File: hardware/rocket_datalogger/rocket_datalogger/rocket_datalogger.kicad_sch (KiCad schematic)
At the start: 8 parts, among them J4 USB_C_Receptacle_USB2.0_14P

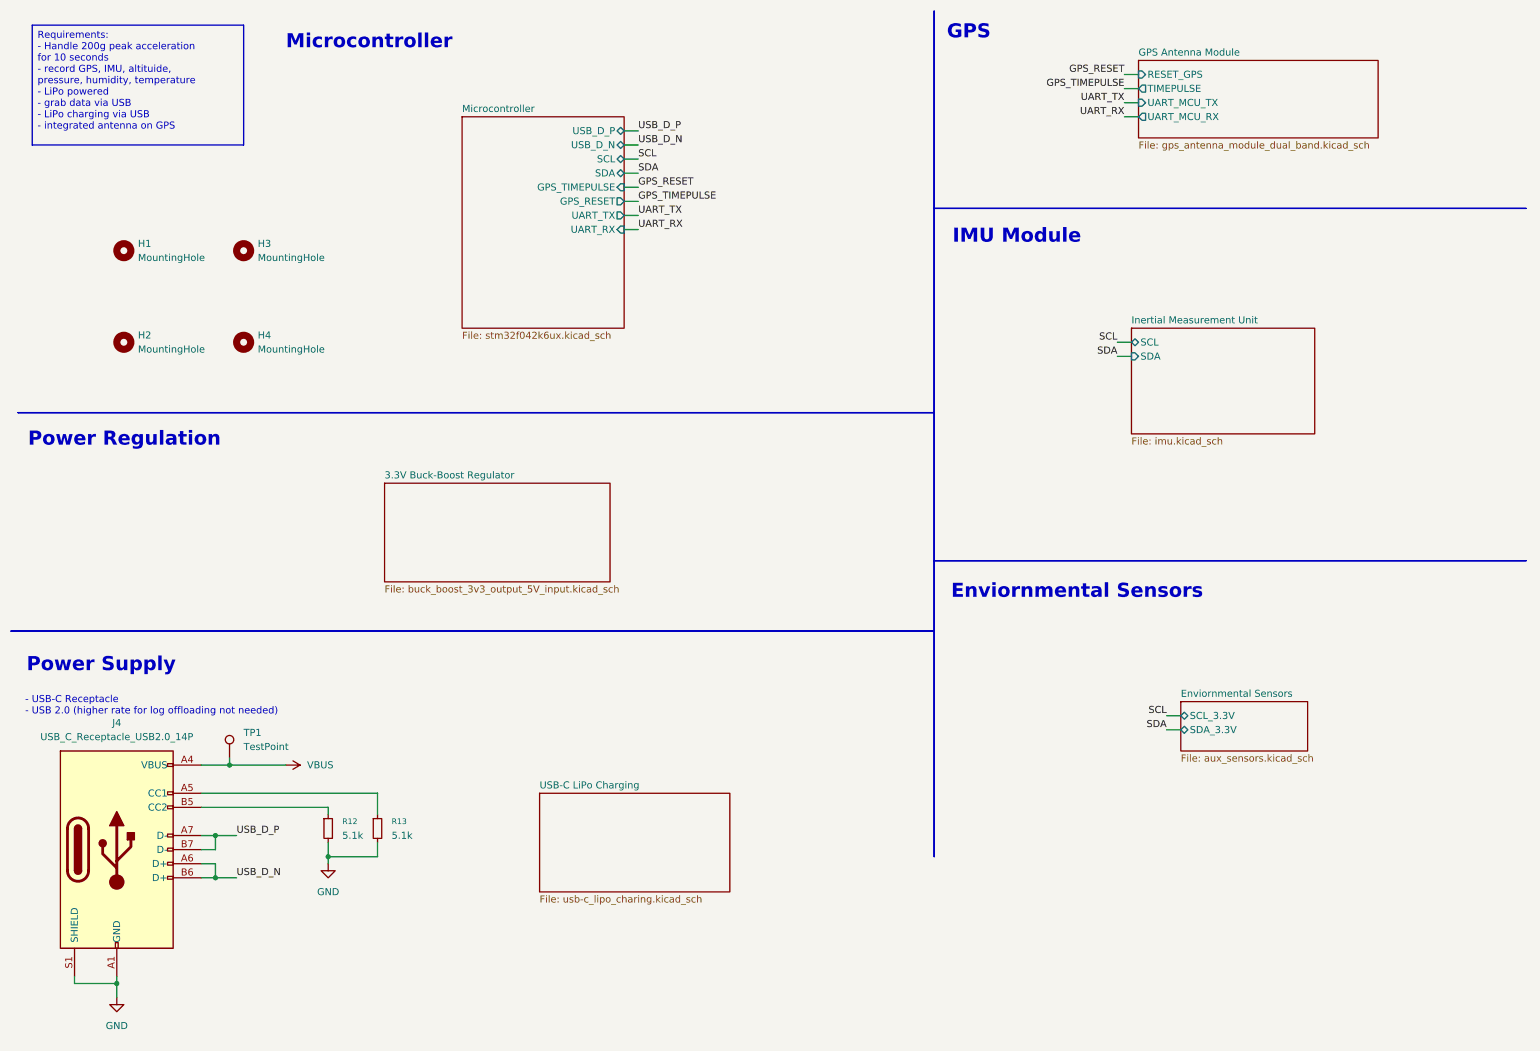
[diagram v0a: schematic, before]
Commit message: Changed IMU to BNO055
Previous IMU required 1.85V rail
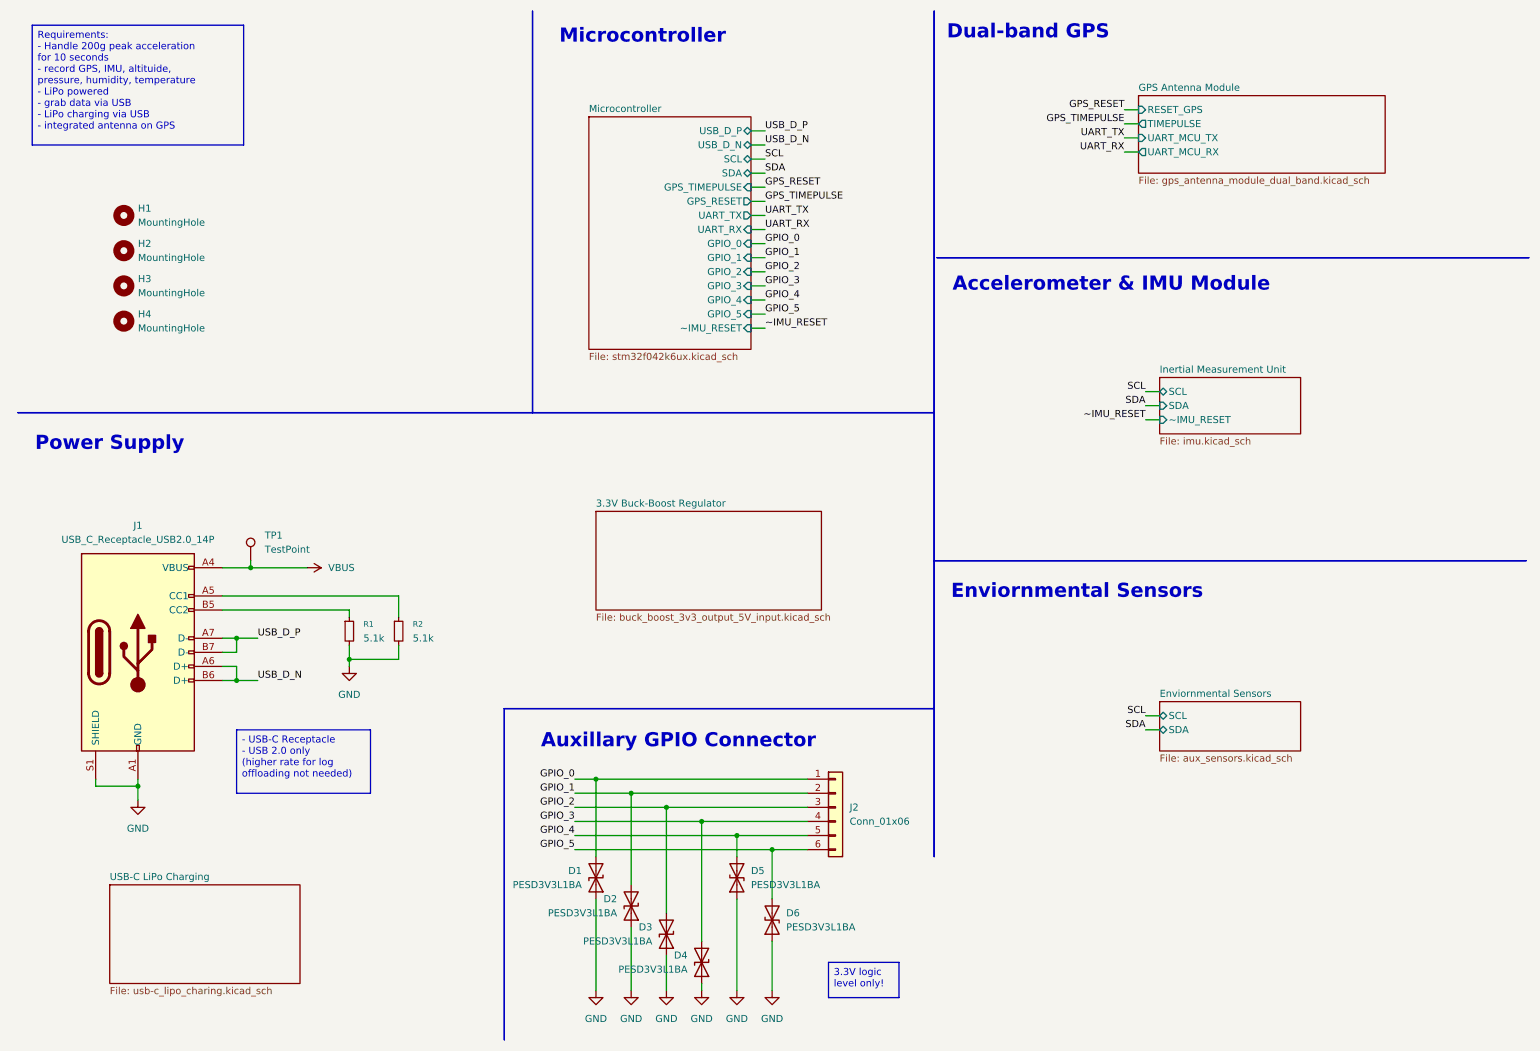
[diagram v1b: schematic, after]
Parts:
- added D1, D2, D3, D4, D5, D6: PESD3V3L1BA, symbol Device:D_TVS
- added J2: Conn_01x06, symbol Connector_Generic:Conn_01x06
- renumbered J4 to J1, R12 to R1, R13 to R2
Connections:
- net GND: now also D1.1 (A1), D2.1 (A1), D3.1 (A1), D4.1 (A1), D5.1 (A1), D6.1 (A1)
- new net GPIO_0: D1.2 (A2), J2.1 (Pin_1)
- new net GPIO_1: D2.2 (A2), J2.2 (Pin_2)
- new net GPIO_2: D3.2 (A2), J2.3 (Pin_3)
- new net GPIO_3: D4.2 (A2), J2.4 (Pin_4)
- new net GPIO_4: D5.2 (A2), J2.5 (Pin_5)
- new net GPIO_5: D6.2 (A2), J2.6 (Pin_6)
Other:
- sheet Enviornmental Sensors ports: added SCL, SDA; removed SCL_3.3V, SDA_3.3V
- sheet Inertial Measurement Unit ports: added ~IMU_RESET; removed none
- sheet Microcontroller ports: added GPIO_0, GPIO_1, GPIO_2, GPIO_3, GPIO_4, GPIO_5, ~IMU_RESET; removed none
- note added: "Accelerometer & IMU Module"
- note added: "Auxillary GPIO Connector"
- note added: "Dual-band GPS"
- note removed: "- USB-C Receptacle - USB 2.0 (higher rate for log offloading not needed)"
- note removed: "GPS"
- note removed: "IMU Module"
- note removed: "Power Regulation"
- moved on the sheet: H1, H2, H3, H4, J1, R1, R2, TP1

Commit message: fixed minor hardware issues
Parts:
- R1, R2: footprint (none) -> Resistor_SMD:R_0603_1608Metric
- TP1: footprint (none) -> TestPoint:TestPoint_Pad_D2.0mm
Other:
- sheet Inertial Measurement Unit ports: added IMU_INT; removed none
- sheet Microcontroller ports: added IMU_INT; removed none
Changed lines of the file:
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@@
+	(wire
+		(pts
+			(xy 147.32 72.39) (xy 144.78 72.39)
+		)
+		(stroke
+			(width 0)
+			(type default)
+		)
+	)
+	(wire
+		(pts
+			(xy 215.9 88.9) (xy 218.44 88.9)
+		)
+		(stroke
+			(width 0)
+			(type default)
+		)
+	)
 	(wire
 		(pts
@@
 		)
 	)
+	(label "IMU_INT"
+		(at 215.9 88.9 180)
+		(effects
+			(font
+				(size 1.27 1.27)
+			)
+			(justify right bottom)
+		)
+	)
 	(label "GPIO_4"
 		(at 113.03 161.29 180)
@@
 	(label "~IMU_RESET"
 		(at 147.32 69.85 0)
+		(effects
+			(font
+				(size 1.27 1.27)
+			)
+			(justify left bottom)
+		)
+	)
+	(label "IMU_INT"
+		(at 147.32 72.39 0)
 		(effects
 			(font
@@
 			)
 		)
-		(property "Footprint" ""
+		(property "Footprint" "TestPoint:TestPoint_Pad_D2.0mm"
 			(at 59.69 111.76 0)
 			(effects
@@
 			)
 		)
-		(property "Footprint" ""
+		(property "Footprint" "Resistor_SMD:R_0603_1608Metric"
 			(at 72.39 124.46 0)
 			(effects
@@
 			)
 		)
-		(property "Footprint" ""
+		(property "Footprint" "Resistor_SMD:R_0603_1608Metric"
 			(at 81.28 124.46 0)
 			(effects
@@
 	(sheet
 		(at 218.44 78.74)
-		(size 25.4 10.16)
+		(size 25.4 13.97)
 		(exclude_from_sim no)
 		(in_bom yes)
@@
 		)
 		(property "Sheetfile" "imu.kicad_sch"
-			(at 218.44 89.4846 0)
+			(at 218.44 93.2946 0)
 			(effects
 				(font
@@
 		(pin "~IMU_RESET" input
 			(at 218.44 86.36 180)
+			(effects
+				(font
+					(size 1.27 1.27)
+				)
+				(justify left)
+			)
+		)
+		(pin "IMU_INT" output
+			(at 218.44 88.9 180)
 			(effects
 				(font
@@
 			(effects
 				(font
+					(size 1.27 1.27)
+				)
+				(justify right)
+			)
+		)
+		(pin "IMU_INT" input
+			(at 144.78 72.39 0)
+			(effects
+				(font

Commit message: Minor revision
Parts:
- D1, D2, D3, D4, D5, D6: footprint (none) -> Diode_SMD:D_SOD-323
- J1: footprint (none) -> Connector_USB:USB_C_Receptacle_GCT_USB4105-xx-A_16P_TopMnt_Horizontal
- J2: value Conn_01x06 -> JST-PH-S6B-SM4_TB; footprint (none) -> Connector_JST:JST_PH_S6B-PH-SM4-TB_1x06-1MP_P2.00mm_Horizontal
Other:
- moved on the sheet: J2
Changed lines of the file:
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@@
 	(wire
 		(pts
-			(xy 154.94 156.21) (xy 129.54 156.21)
+			(xy 148.59 156.21) (xy 129.54 156.21)
 		)
 		(stroke
@@
 	(wire
 		(pts
-			(xy 154.94 161.29) (xy 142.24 161.29)
+			(xy 148.59 161.29) (xy 142.24 161.29)
 		)
 		(stroke
@@
 	(wire
 		(pts
-			(xy 154.94 158.75) (xy 135.89 158.75)
+			(xy 148.59 158.75) (xy 135.89 158.75)
 		)
 		(stroke
@@
 	(wire
 		(pts
-			(xy 154.94 153.67) (xy 123.19 153.67)
+			(xy 148.59 153.67) (xy 123.19 153.67)
 		)
 		(stroke
@@
 	(wire
 		(pts
-			(xy 154.94 163.83) (xy 148.59 163.83)
-		)
-		(stroke
-			(width 0)
-			(type default)
-		)
-	)
-	(wire
-		(pts
 			(xy 81.28 127) (xy 81.28 129.54)
 		)
@@
 	(wire
 		(pts
-			(xy 154.94 151.13) (xy 116.84 151.13)
+			(xy 148.59 151.13) (xy 116.84 151.13)
 		)
 		(stroke
@@
 			)
 		)
-		(property "Footprint" ""
+		(property "Footprint" "Diode_SMD:D_SOD-323"
 			(at 148.59 176.53 0)
 			(effects
@@
 			)
 		)
-		(property "Footprint" ""
+		(property "Footprint" "Diode_SMD:D_SOD-323"
 			(at 123.19 173.99 0)
 			(effects
@@
 			)
 		)
-		(property "Footprint" ""
+		(property "Footprint" "Diode_SMD:D_SOD-323"
 			(at 116.84 168.91 0)
 			(effects
@@
 			)
 		)
-		(property "Footprint" ""
+		(property "Footprint" "Diode_SMD:D_SOD-323"
 			(at 135.89 184.15 0)
 			(effects
@@
 			)
 		)
-		(property "Footprint" ""
+		(property "Footprint" "Connector_USB:USB_C_Receptacle_GCT_USB4105-xx-A_16P_TopMnt_Horizontal"
 			(at 38.1 128.27 0)
 			(effects
@@
 	(symbol
 		(lib_id "Connector_Generic:Conn_01x06")
-		(at 160.02 156.21 0)
+		(at 153.67 156.21 0)
 		(unit 1)
 		(exclude_from_sim no)
@@
 		(fields_autoplaced yes)
 		(property "Reference" "J2"
-			(at 162.56 156.2099 0)
+			(at 156.21 156.2099 0)
 			(effects
 				(font
@@
 			)
 		)
-		(property "Value" "Conn_01x06"
-			(at 162.56 158.7499 0)
+		(property "Value" "JST-PH-S6B-SM4_TB"
+			(at 156.21 158.7499 0)
 			(effects
 				(font
@@
 			)
 		)
-		(property "Footprint" ""
-			(at 160.02 156.21 0)
+		(property "Footprint" "Connector_JST:JST_PH_S6B-PH-SM4-TB_1x06-1MP_P2.00mm_Horizontal"
+			(at 153.67 156.21 0)
 			(effects
 				(font
@@
 		)
 		(property "Datasheet" "~"
-			(at 160.02 156.21 0)
+			(at 153.67 156.21 0)
 			(effects
 				(font
@@
 		)
 		(property "Description" "Generic connector, single row, 01x06, script generated (kicad-library-utils/schlib/autogen/connector/)"
-			(at 160.02 156.21 0)
+			(at 153.67 156.21 0)
 			(effects
 				(font
@@
 			)
 		)
-		(property "Footprint" ""
+		(property "Footprint" "Diode_SMD:D_SOD-323"
 			(at 142.24 168.91 0)
 			(effects
@@
 			)
 		)
-		(property "Footprint" ""
+		(property "Footprint" "Diode_SMD:D_SOD-323"
 			(at 129.54 179.07 0)
 			(effects

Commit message: PCB design rev 1
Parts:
- removed J1: USB_C_Receptacle_USB2.0_14P, Connector_USB:USB_C_Receptacle_GCT_USB4105-xx-A_16P_TopMnt_Horizontal, symbol Connector:USB_C_Receptacle_USB2.0_14P
- added J5: USB_C_Receptacle_USB2.0_16P, Connector_USB:USB_C_Receptacle_GCT_USB4105-xx-A_16P_TopMnt_Horizontal, symbol Connector:USB_C_Receptacle_USB2.0_16P
- added J6: JST-PH-S6B-SM4_TB, Connector_JST:JST_PH_S6B-PH-SM4-TB_1x06-1MP_P2.00mm_Horizontal, symbol Connector_Generic:Conn_01x06
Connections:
- net GND: now also J5.A1 (GND), J5.A12 (GND), J5.B1 (GND), J5.B12 (GND), J5.S1 (SHIELD), J6.1 (Pin_1)
- net GPS_RESET: now also J6.5 (Pin_5)
- net GPS_TIMEPULSE: now also J6.4 (Pin_4)
- net UART_RX: now also J6.3 (Pin_3)
- net UART_TX: now also J6.2 (Pin_2)
- net USB_D_N: now also J5.A6 (D+), J5.B6 (D+)
- net USB_D_P: now also J5.A7 (D-), J5.B7 (D-)
- net VBUS: now also J5.A4 (VBUS), J5.A9 (VBUS), J5.B4 (VBUS), J5.B9 (VBUS)
- net at R2.1: now also J5.A5 (CC1)
- net at R1.1: now also J5.B5 (CC2)
- new net +3.3V: J6.6 (Pin_6)
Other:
- removed sheet GPS Antenna Module
- sheet Microcontroller ports: added UART_MCU_RX, UART_MCU_TX; removed UART_RX, UART_TX
- note added: "GPS needs 90 deg rotated PCB facing the sky for ideal placement"

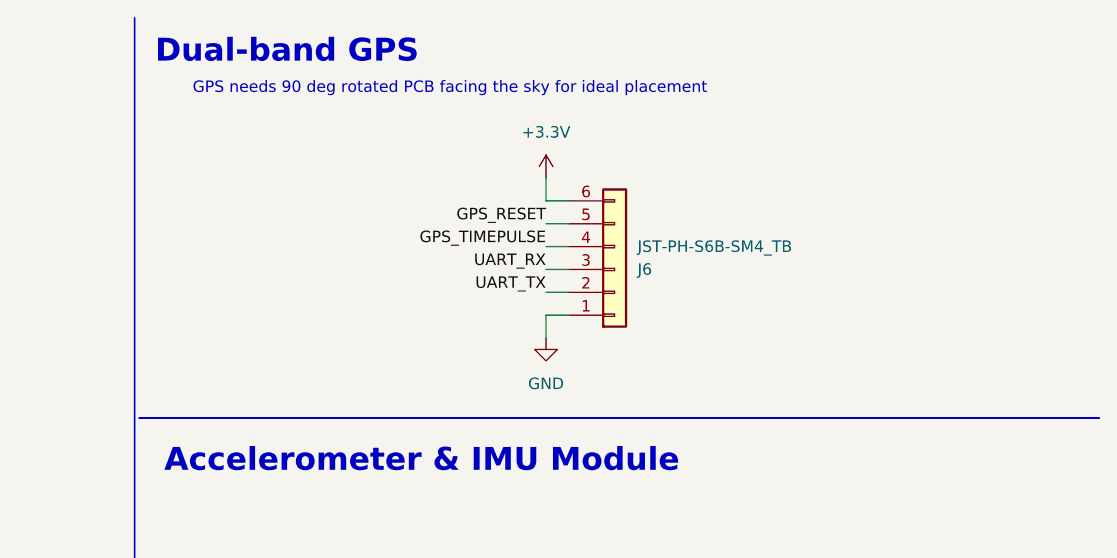
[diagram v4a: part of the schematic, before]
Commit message: Updated BOM and schematic notes
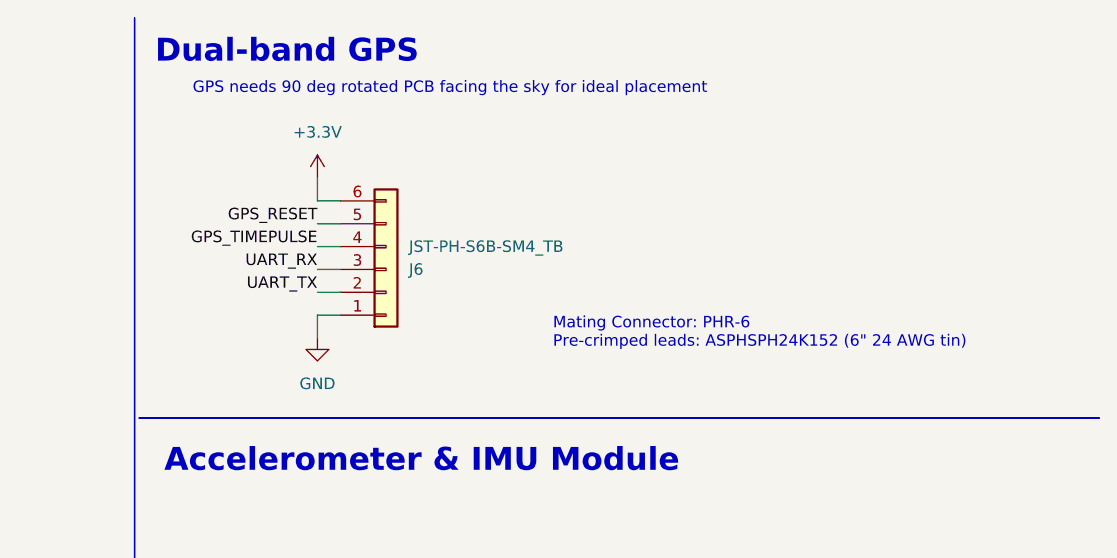
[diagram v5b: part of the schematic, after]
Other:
- note added: "Mating Connector: PHR-6 Pre-crimped leads: ASPHSPH24K152 (6" 24 AWG tin)"
- moved on the sheet: J6
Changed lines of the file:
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@@
+		)
+	)
+	(text "Mating Connector: PHR-6\nPre-crimped leads: ASPHSPH24K152 (6\" 24 AWG tin)"
+		(exclude_from_sim no)
+		(at 224.282 47.752 0)
+		(effects
+			(font
+				(size 1.27 1.27)
+			)
+			(justify left)
 		)
 	)
@@
 	(wire
 		(pts
-			(xy 223.52 33.02) (xy 226.06 33.02)
+			(xy 198.12 33.02) (xy 200.66 33.02)
 		)
 		(stroke
@@
 	(wire
 		(pts
-			(xy 223.52 38.1) (xy 226.06 38.1)
+			(xy 198.12 38.1) (xy 200.66 38.1)
 		)
 		(stroke
@@
 	(wire
 		(pts
-			(xy 223.52 35.56) (xy 226.06 35.56)
+			(xy 198.12 35.56) (xy 200.66 35.56)
 		)
 		(stroke
@@
 	(wire
 		(pts
-			(xy 223.52 45.72) (xy 226.06 45.72)
+			(xy 198.12 45.72) (xy 200.66 45.72)
 		)
 		(stroke
@@
 	(wire
 		(pts
-			(xy 223.52 40.64) (xy 226.06 40.64)
+			(xy 198.12 40.64) (xy 200.66 40.64)
 		)
 		(stroke
@@
 	(wire
 		(pts
-			(xy 223.52 43.18) (xy 226.06 43.18)
+			(xy 198.12 43.18) (xy 200.66 43.18)
 		)
 		(stroke
@@
 	(wire
 		(pts
-			(xy 223.52 30.48) (xy 223.52 33.02)
+			(xy 198.12 30.48) (xy 198.12 33.02)
 		)
 		(stroke
@@
 	(wire
 		(pts
-			(xy 223.52 45.72) (xy 223.52 48.26)
+			(xy 198.12 45.72) (xy 198.12 48.26)
 		)
 		(stroke
@@
 	)
 	(label "UART_RX"
-		(at 223.52 40.64 180)
+		(at 198.12 40.64 180)
 		(effects
 			(font
@@
 	)
 	(label "GPS_RESET"
-		(at 223.52 35.56 180)
+		(at 198.12 35.56 180)
 		(effects
 			(font
@@
 	)
 	(label "UART_TX"
-		(at 223.52 43.18 180)
+		(at 198.12 43.18 180)
 		(effects
 			(font
@@
 	)
 	(label "GPS_TIMEPULSE"
-		(at 223.52 38.1 180)
+		(at 198.12 38.1 180)
 		(effects
 			(font
@@
 	(symbol
 		(lib_id "power:GND")
-		(at 223.52 48.26 0)
+		(at 198.12 48.26 0)
 		(unit 1)
 		(exclude_from_sim no)
@@
 		(fields_autoplaced yes)
 		(property "Reference" "#PWR071"
-			(at 223.52 54.61 0)
+			(at 198.12 54.61 0)
 			(effects
 				(font
@@
 		)
 		(property "Value" "GND"
-			(at 223.52 53.34 0)
+			(at 198.12 53.34 0)
 			(effects
 				(font
@@
 		)
 		(property "Footprint" ""
-			(at 223.52 48.26 0)
+			(at 198.12 48.26 0)
 			(effects
 				(font
@@
 		)
 		(property "Datasheet" ""
-			(at 223.52 48.26 0)
+			(at 198.12 48.26 0)
 			(effects
 				(font
@@
 		)
 		(property "Description" "Power symbol creates a global label with name \"GND\" , ground"
-			(at 223.52 48.26 0)
+			(at 198.12 48.26 0)
 			(effects
 				(font
@@
 	(symbol
 		(lib_id "Connector_Generic:Conn_01x06")
-		(at 231.14 40.64 0)
+		(at 205.74 40.64 0)
 		(mirror x)
 		(unit 1)
@@
 		(dnp no)
 		(property "Reference" "J6"
-			(at 233.68 40.6401 0)
+			(at 208.28 40.6401 0)
 			(effects
 				(font
@@
 		)
 		(property "Value" "JST-PH-S6B-SM4_TB"
-			(at 233.68 38.1001 0)
+			(at 208.28 38.1001 0)
 			(effects
 				(font
@@
 		)
 		(property "Footprint" "Connector_JST:JST_PH_S6B-PH-SM4-TB_1x06-1MP_P2.00mm_Horizontal"
-			(at 231.14 40.64 0)
+			(at 205.74 40.64 0)
 			(effects
 				(font
@@
 		)
 		(property "Datasheet" "~"
-			(at 231.14 40.64 0)
+			(at 205.74 40.64 0)
 			(effects
 				(font
@@
 		)
 		(property "Description" "Generic connector, single row, 01x06, script generated (kicad-library-utils/schlib/autogen/connector/)"
-			(at 231.14 40.64 0)
+			(at 205.74 40.64 0)
 			(effects
 				(font
@@
 	(symbol
 		(lib_id "power:+3.3V")
-		(at 223.52 30.48 0)
+		(at 198.12 30.48 0)
 		(unit 1)
 		(exclude_from_sim no)
@@
 		(fields_autoplaced yes)
 		(property "Reference" "#PWR072"
-			(at 223.52 34.29 0)
+			(at 198.12 34.29 0)
 			(effects
 				(font
@@
 		)
 		(property "Value" "+3.3V"
-			(at 223.52 25.4 0)
+			(at 198.12 25.4 0)
 			(effects
 				(font
@@
 		)
 		(property "Footprint" ""
-			(at 223.52 30.48 0)
+			(at 198.12 30.48 0)
 			(effects
 				(font
@@
 		)
 		(property "Datasheet" ""
-			(at 223.52 30.48 0)
+			(at 198.12 30.48 0)
 			(effects
 				(font
@@
 		)
 		(property "Description" "Power symbol creates a global label with name \"+3.3V\""
-			(at 223.52 30.48 0)
-			(effects
-				(font
+			(at 198.12 30.48 0)
+			(effects
+				(font
